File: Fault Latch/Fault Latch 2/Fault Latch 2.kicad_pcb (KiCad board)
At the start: 2 copper layers, 110 x 90 mm, 108 parts, among them K101 Fujitsu_FTR-LYAA005x, K102 Fujitsu_FTR-LYAA005x, K103 Fujitsu_FTR-LYAA005x, Q101 Q_NPN_BEC, Q102 Q_NPN_BEC, Q103 Q_NPN_BEC, Q104 Q_NPN_BEC, Q105 Q_NMOS_GSD, Q106 Q_NMOS_GSD, Q107 Q_PMOS_GSD, Q108 Q_PMOS_GSD, Q109 Q_NMOS_GDS, Q110 Q_NPN_BEC, Q111 Q_NPN_BEC, Q112 Q_NMOS_GSD, Q113 Q_PMOS_GSD, SW101 SW_Omron_B3FS, SW102 SW_Omron_B3FS, SW103 SW_Omron_B3FS, U101 SFH617A-1, U102 SFH617A-1, U103 SFH617A-1, U104 74AHC1G00, U105 74AHC1G00, U106 74AHC1G00, U107 74LS279, U108 641964-1, U109 SFH617A-1, U110 SFH617A-1, U111 641964-1, U112 641964-1, U113 641964-1, U114 641964-1, U115 641964-1, U116 641964-1, U117 74AHC1G00, U118 LM555xM, U119 74AHC1G00, U120 641964-1, U121 SFH617A-1, U122 641964-1

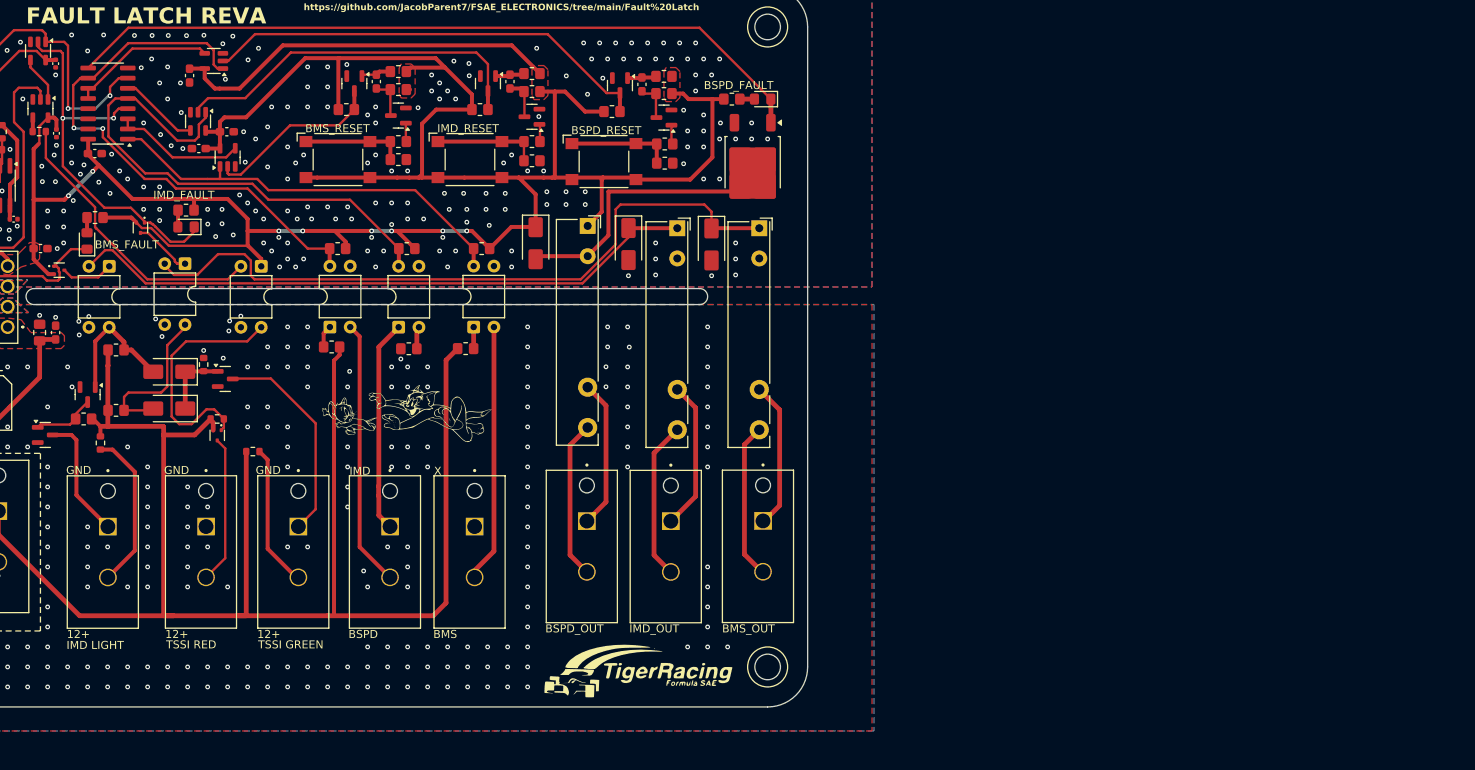
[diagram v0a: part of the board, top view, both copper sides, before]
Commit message: Fault Latch - THT
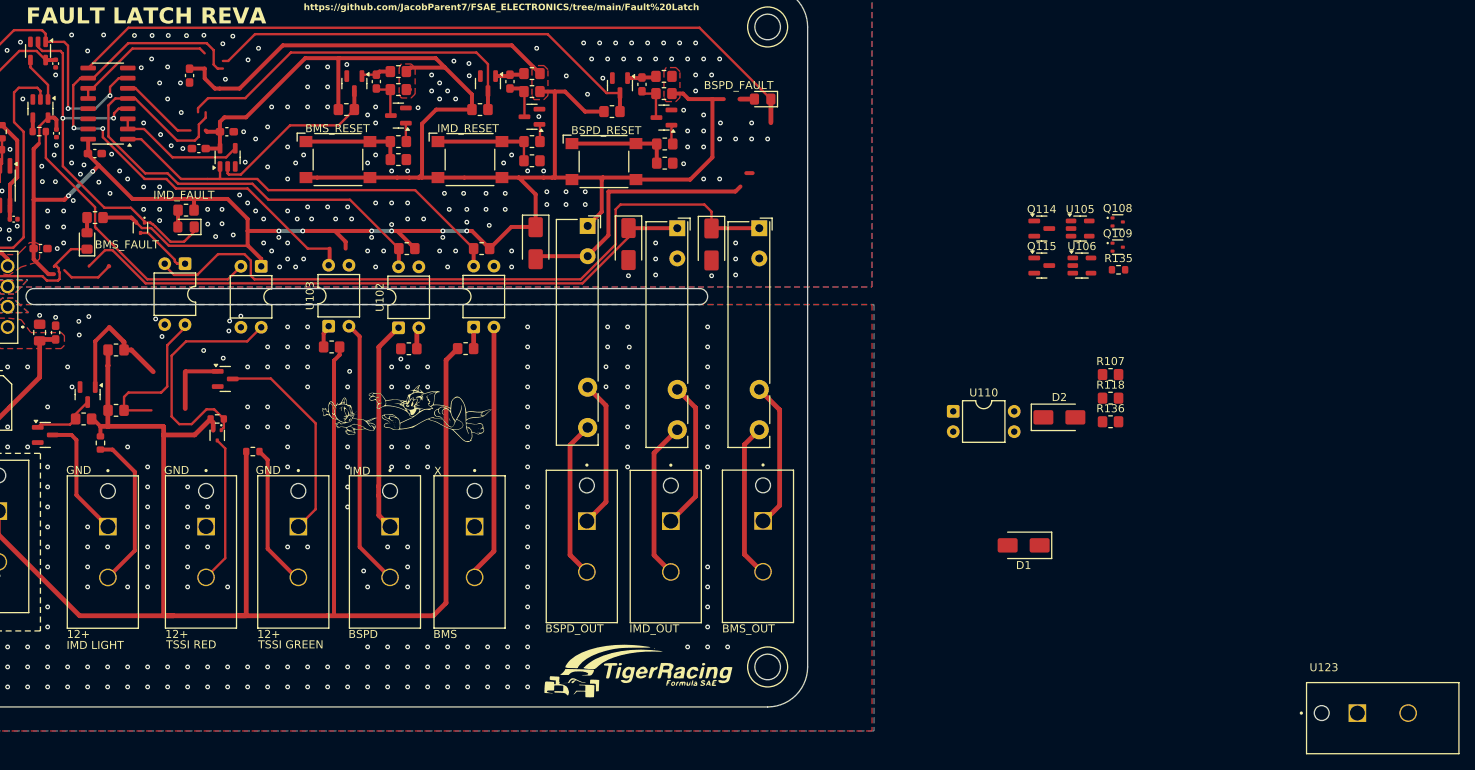
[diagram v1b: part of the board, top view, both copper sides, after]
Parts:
- removed D107, D108: D_Schottky, Diode_SMD:D_SMA
- removed R128: 10k, Resistor_SMD:R_0603_1608Metric
- added D1: SS12, Diode_SMD:D_SMA, F.Cu at (206.2, 113.9)
- added D2: SS12, Diode_SMD:D_SMA, F.Cu at (210.7, 97.9)
- added Q114: Q_NMOS_GSD, Package_TO_SOT_SMD:SOT-23, F.Cu at (208.5, 74.3)
- added Q115: Q_NMOS_GSD, Package_TO_SOT_SMD:SOT-23, F.Cu at (208.5, 78.9)
- added R135: 510R, Resistor_SMD:R_0603_1608Metric, F.Cu at (218.1, 79.4)
- added R136: 10k, Resistor_SMD:R_0805_2012Metric_Pad1.20x1.40mm_HandSolder, F.Cu at (217.1, 98.4)
- added U123: 641964-1, 641964-1:TE_641964-1, F.Cu at (247.9, 134.8)
- Q109: value Q_NMOS_GDS -> Q_PMOS_GSD; footprint Package_TO_SOT_SMD:TO-252-2 -> Package_TO_SOT_SMD:SOT-523
- R103: value 2.2k -> 10k
- R106, R107, R109: value 10k -> 1k
- R112: value 500R -> 510R
- R116, R117, R118: value 270R -> 2k
- moved Q108 132.4 mm to (218.0, 73.4)
- moved U106 111.5 mm to (213.5, 78.9), turned to 0 degrees
- moved U105 111.1 mm to (213.3, 74.3), turned to 0 degrees
- moved U110 107.0 mm to (197.4, 97.1), turned to 0 degrees
- moved R107 97.9 mm to (217.1, 92.5), turned to 0 degrees
- moved R118 60.3 mm to (217.1, 95.5), turned to 0 degrees
- moved Q109 46.8 mm to (218.0, 76.6), turned to 0 degrees
- moved U103 0.19 mm to (119.3, 86.5)
- moved U102 0.07 mm to (128.1, 86.7)
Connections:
- C113 pad 1: GNDPWR -> +12V
- C113 pad 2: +12V -> GNDPWR
- C114 pad 1: GNDPWR -> +12V
- C114 pad 2: +12V -> GNDPWR
- C115 pad 1: GNDPWR -> +12V
- C115 pad 2: +12V -> GNDPWR
- D105 pad 1: +5V -> Net-(D105-K)
- D105 pad 2: Net-(D105-A) -> GND
- K102 pad A1: +5V -> Net-(D105-K)
- K102 pad A2: Net-(D105-A) -> GND
- PS101 pad 1: +12V -> GNDPWR
- PS101 pad 2: GNDPWR -> +12V
- Q109 pad 2: Net-(D105-A) -> +5V
- Q109 pad 3: GND -> Net-(D105-K)
- R103 pad 1: Net-(R103-Pad1) -> +12V
- R103 pad 2: GNDPWR -> Net-(R103-Pad2)
- U102 pad 1: /IMD_HV -> Net-(R103-Pad2)
- U102 pad 2: Net-(R103-Pad1) -> /IMD_HV
- U120 pad 1: +12V -> GNDPWR
- U120 pad 2: GNDPWR -> +12V
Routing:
- net Net-(D105-A): track 33.4 -> 0.00 mm
- net GND: track 0.00 -> 32.6 mm
- net +12V: track 231.8 -> 234.6 mm
- net Net-(R103-Pad1): track 2.80 -> 0.00 mm
- net (no net): track 0.00 -> 0.80 mm

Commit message: Revised Fault Latch Layout
Fixed the schematic, did layout and wiring. Check for size and missed wires.
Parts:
- removed PS101: RI-1205S, DC-DC:RI0505S
- removed U108, U111, U112, U113, U114, U115, U116, U120, U123: 641964-1, 641964-1:TE_641964-1
- added J1: 1053141312, footprints:CONN_SD-105314-100_12_MOL, F.Cu at (-296.9, -371.2)
- added J2: 1053141106, molex.6-pin.footprint:CONN_SD-105314-100_06_MOL, F.Cu at (-301.6, -351.1)
- added J3: 1053131202, molex.2-pin.footprint:CONN_SD-105313-100_02_MOL, F.Cu at (-427.0, -311.3)
- added R137: 10k, Resistor_SMD:R_0805_2012Metric_Pad1.20x1.40mm_HandSolder, F.Cu at (-321.7, -358.5)
- added U1: LM1117DTX-5.0_NOPB, LM1117DTX-5.0_NOPB:TO228P970X238-3N, F.Cu at (-322.4, -324.9)
- R102, R103: value 10k -> 220; footprint Resistor_SMD:R_0805_2012Metric_Pad1.20x1.40mm_HandSolder -> Resistor_SMD:R_0201_0603Metric
- R104, R133: value 10k -> 220
- moved R107 739.7 mm to (-388.8, -331.7), turned to -90 degrees
- moved U105 731.8 mm to (-383.6, -349.2)
- moved R118 719.1 mm to (-361.6, -331.4), turned to 90 degrees
- moved U106 718.7 mm to (-382.8, -322.2)
- moved R136 712.7 mm to (-311.2, -380.0), turned to -90 degrees
- moved Q108 711.2 mm to (-353.1, -350.5)
- moved D1 711.2 mm to (-328.7, -354.8), turned to 0 degrees
- moved SW103 707.9 mm to (-433.8, -329.0), turned to 180 degrees
- moved R102 706.7 mm to (-398.1, -373.0), turned to 90 degrees
- moved R122 706.6 mm to (-429.3, -321.7), turned to -90 degrees
- moved U110 705.6 mm to (-348.0, -350.5)
- moved SW102 705.3 mm to (-433.0, -349.7), turned to 180 degrees
- moved SW101 705.3 mm to (-432.8, -371.7), turned to 180 degrees
- moved R123 704.6 mm to (-425.3, -326.5)
- moved R113 704.4 mm to (-429.0, -342.7), turned to -90 degrees
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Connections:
- C113 pad 2: GNDPWR -> GND
- C114 pad 2: GNDPWR -> GND
- C115 pad 2: GNDPWR -> GND
- K101 pad 13: Net-(K101-Pad13) -> /BMS Out
- K101 pad 14: Net-(K101-Pad14) -> /Shutdown Circuit In
- K102 pad 13: Net-(K102-Pad13) -> /Shutdown Circuit Out
- K102 pad 14: Net-(K102-Pad14) -> unconnected-(K102-Pad14)
- K103 pad 13: Net-(K103-Pad13) -> /IMD Out
- K103 pad 14: Net-(K103-Pad14) -> /IMD In
- Q105 pad 2: GNDPWR -> GND
- Q106 pad 2: GNDPWR -> GND
- Q106 pad 3: Net-(Q106-D) -> /IMD Light Out
- Q112 pad 2: GNDPWR -> GND
- Q112 pad 3: Net-(Q112-D) -> /TSSI Green Out
- Q114 pad 1: /BMS_GREEN -> /BMS_Green
- Q114 pad 2: GNDPWR -> GND
- Q115 pad 2: GNDPWR -> GND
- Q115 pad 3: Net-(Q115-D) -> /BMS Light Out
- R112 pad 2: Net-(R112-Pad2) -> /IMD Light In
- R130 pad 1: Net-(R130-Pad1) -> /TSSI Green In
- R135 pad 2: Net-(R135-Pad2) -> /BMS Light In
- U109 pad 3: GNDPWR -> GND
- U110 pad 3: GNDPWR -> GND
- U121 pad 3: GNDPWR -> GND
- U122 pad 1: GNDPWR -> GND
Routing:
- net +12V: track 234.6 -> 394.4 mm, vias 0 -> 31
- net /Shutdown Circuit Out: track 0.00 -> 85.8 mm
- net Net-(D104-K): track 87.5 -> 15.2 mm
- net Net-(D106-K): track 79.7 -> 16.9 mm
- net Net-(D103-K): track 94.1 -> 33.3 mm
- net +5V: track 406.5 -> 455.4 mm, vias 8 -> 28
- net /CLOCK: track 43.4 -> 88.8 mm
- net /TSSI Green Out: track 0.00 -> 43.4 mm, vias 0 -> 7
- net /BMS_SR: track 48.6 -> 90.8 mm, vias 2 -> 4
- net /NIMD_LV: track 65.6 -> 24.8 mm
- net /BMS Out: track 0.00 -> 37.3 mm, vias 0 -> 2
- net /IMD Out: track 0.00 -> 34.6 mm
- net /IMD Light Out: track 0.00 -> 34.2 mm, vias 0 -> 2
- net /BSPD_HV: track 33.4 -> 0.00 mm
- net GND: track 32.6 -> 0.00 mm, vias 218 -> 0
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- removed copper zone on B.Cu, net GNDPWR
- removed copper zone on F.Cu, net GNDPWR
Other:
- board size 110 x 90 mm -> 625.1 x 519.7 mm

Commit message: Fault Latch Layout revised
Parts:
- removed U1: LM1117DTX-5.0_NOPB, LM1117DTX-5.0_NOPB:TO228P970X238-3N
- removed U122: 641964-1, 641964-1:TE_641964-1
- added Q116: Q_NMOS_GSD, Package_TO_SOT_SMD:SOT-23, F.Cu at (230.8, 95.5)
- added R138: 10k, Resistor_SMD:R_0805_2012Metric_Pad1.20x1.40mm_HandSolder, F.Cu at (230.8, 100.2)
- added U2: LM1117DT-5.0, Package_TO_SOT_SMD:TO-252-3_TabPin2, F.Cu at (251.7, 118.0)
- R104: footprint Resistor_SMD:R_0805_2012Metric_Pad1.20x1.40mm_HandSolder -> Resistor_SMD:R_0201_0603Metric
- moved H101 873.7 mm to (270.4, 125.3)
- moved SW102 834.7 mm to (268.2, 103.1), turned to 90 degrees
- moved R114 828.8 mm to (265.7, 110.8), turned to 90 degrees
- moved SW101 823.3 mm to (268.1, 60.4), turned to 90 degrees
- moved R113 821.4 mm to (265.7, 95.5), turned to 90 degrees
- moved Q103 820.1 mm to (261.6, 110.7), turned to 180 degrees
- moved R115 819.4 mm to (261.6, 107.3), turned to 180 degrees
- moved R101 818.0 mm to (265.7, 67.7)
- moved C105 813.9 mm to (262.8, 103.6), turned to 90 degrees
- moved SW103 813.1 mm to (268.1, 81.5), turned to 90 degrees
- moved R119 811.0 mm to (261.6, 100.3), turned to 180 degrees
- moved R105 809.3 mm to (265.7, 53.0), turned to -90 degrees
- moved R123 806.3 mm to (265.7, 88.9), turned to 90 degrees
- moved R108 804.5 mm to (261.7, 55.9), turned to 180 degrees
- moved Q104 803.9 mm to (261.8, 96.9), turned to 90 degrees
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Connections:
- J1 pad 1: /NBMS HV -> GND
- J1 pad 10: /TSSI Red In -> /BPSD HV
- J1 pad 11: /TSSI Red Out -> /IMD HV
- J1 pad 12: unconnected-(J1-Pad12) -> /NBMS HV
- J1 pad 2: /IMD HV -> /BMS Light Out
- J1 pad 3: /BPSD HV -> /TSSI Green Out
- J1 pad 4: /BMS Light In -> /TSSI Green In
- J1 pad 5: /BMS Light Out -> /IMD Light Out
- J1 pad 7: /IMD Light Out -> unconnected-(J1-Pad7)
- J1 pad 8: /TSSI Green In -> /TSSI Red In
- J1 pad 9: /TSSI Green Out -> /BMS Light In
- J3 pad 1: +12V -> GND
- J3 pad 2: GND -> +12V
- K102 pad 14: unconnected-(K102-Pad14) -> /BPSD In
- Q112 pad 1: Net-(D1-A) -> Net-(Q112-G)
- Q113 pad 3: Net-(Q113-D) -> /TSSI Red In
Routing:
- net +12V: track 394.4 -> 202.0 mm, vias 31 -> 3
- net /CLOCK: track 88.8 -> 17.9 mm
- net /Shutdown Circuit Out: track 85.8 -> 36.4 mm
- net /BMS_Green: track 32.8 -> 79.2 mm
- net /TSSI Green Out: track 43.4 -> 4.45 mm, vias 7 -> 0
- net /Shutdown Circuit In: track 31.2 -> 65.2 mm, vias 2 -> 0
- net /BMS_SR: track 90.8 -> 59.4 mm, vias 4 -> 2
- net Net-(U106-Pad4): track 35.9 -> 4.56 mm, vias 2 -> 0
- net /IMD Light Out: track 34.2 -> 4.51 mm, vias 2 -> 0
- net /BPSD In: track 0.00 -> 28.1 mm
- net +5V: track 455.4 -> 430.5 mm, vias 28 -> 5
- net /IMD In: track 19.9 -> 41.0 mm
- net /BMS Out: track 37.3 -> 55.5 mm, vias 2 -> 0
- net Net-(U104-Pad4): track 22.1 -> 5.05 mm
- net /BMS Light Out: track 21.5 -> 5.02 mm, vias 2 -> 0
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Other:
- board size 625.1 x 519.7 mm -> 85 x 85 mm
- board text added: "FAULT LATCH"
- board text removed: "FAULT LATCH REVA"

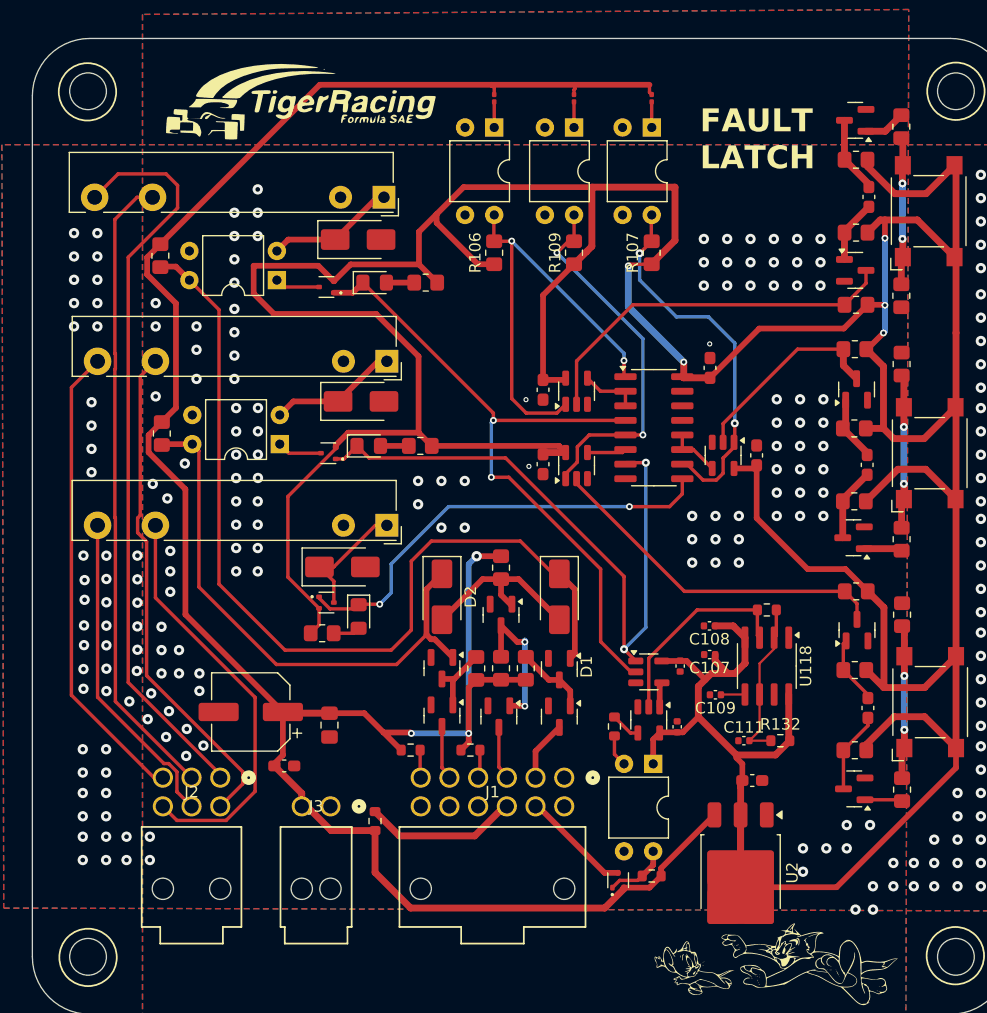
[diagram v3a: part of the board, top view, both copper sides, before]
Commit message: Fault Latch Updates
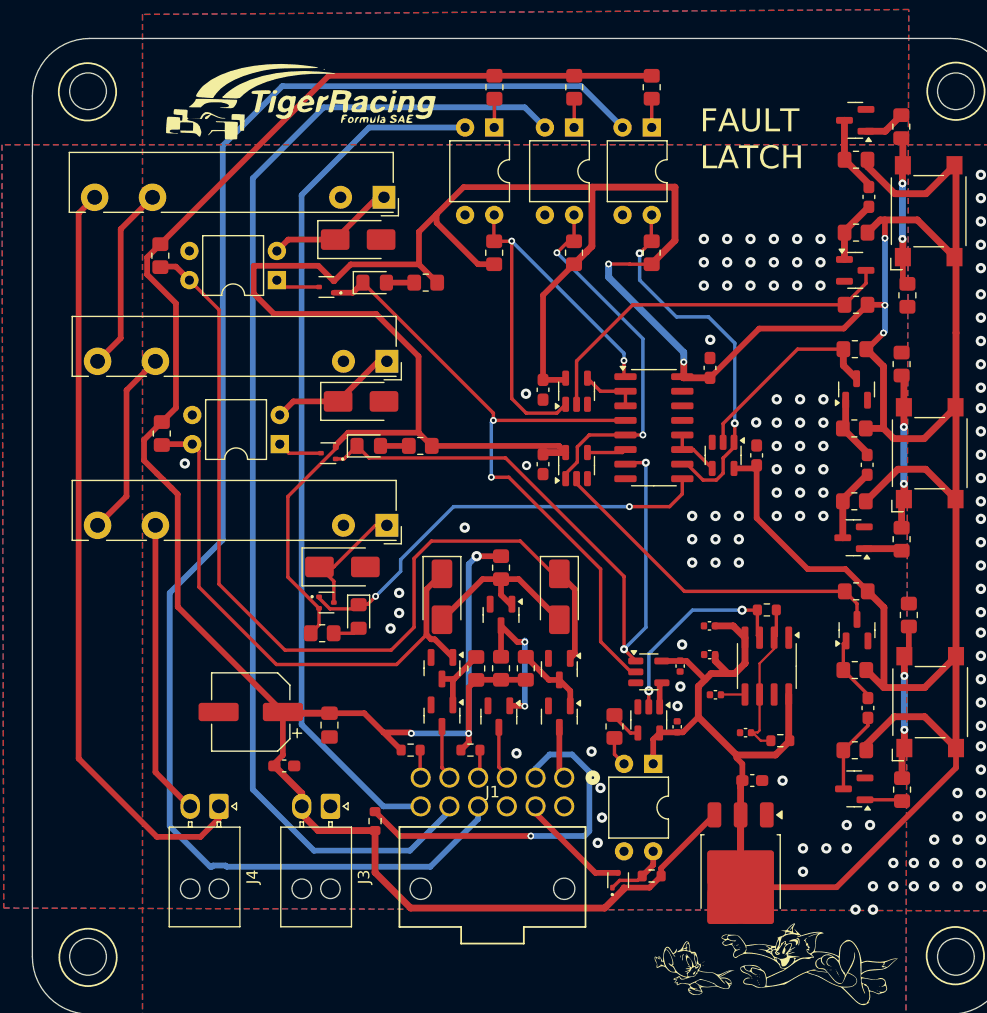
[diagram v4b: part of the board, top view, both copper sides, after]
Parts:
- removed J2: 1053141106, molex.6-pin.footprint:CONN_SD-105314-100_06_MOL
- added J4: 1053131202, Connector_Molex:Molex_Nano-Fit_105313-xx02_1x02_P2.50mm_Horizontal, F.Cu at (206.2, 112.2)
- J3: footprint molex.2-pin.footprint:CONN_SD-105313-100_02_MOL -> Connector_Molex:Molex_Nano-Fit_105313-xx02_1x02_P2.50mm_Horizontal
- R102, R103, R104: footprint Resistor_SMD:R_0201_0603Metric -> Resistor_SMD:R_0805_2012Metric_Pad1.20x1.40mm_HandSolder
- R133: footprint Resistor_SMD:R_0603_1608Metric -> Resistor_SMD:R_0805_2012Metric_Pad1.20x1.40mm_HandSolder
- moved R103 0.95 mm to (237.2, 49.6)
- moved R102 0.95 mm to (230.2, 49.6)
- moved R104 0.95 mm to (243.9, 49.6)
- moved C111 0.71 mm to (252.1, 105.8)
- moved R113 0.59 mm to (266.3, 95.5)
- moved R101 0.53 mm to (266.2, 67.7)
- turned J3 to -90 degrees
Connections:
- J1 pad 1: GND -> /BMS Light Out
- J1 pad 10: /BPSD HV -> /BSPD_HV
- J1 pad 11: /IMD HV -> /IMD_HV
- J1 pad 12: /NBMS HV -> /NBMS_HV
- J1 pad 2: /BMS Light Out -> /BMS Light In
- J1 pad 7: unconnected-(J1-Pad7) -> GND
- J1 pad 9: /BMS Light In -> unconnected-(J1-Pad9)
- K101 pad 13: /BMS Out -> Net-(K101-Pad13)
- K102 pad 14: /BPSD In -> Net-(K102-Pad14)
- K103 pad 13: /IMD Out -> Net-(K102-Pad14)
- K103 pad 14: /IMD In -> Net-(K101-Pad13)
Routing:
- net /BSPD_HV: track 0.00 -> 130.9 mm
- net /IMD_HV: track 0.00 -> 103.2 mm
- net /NBMS_HV: track 0.00 -> 76.1 mm
- net /BMS Out: track 55.5 -> 0.00 mm
- net /IMD Out: track 44.0 -> 0.00 mm
- net /IMD In: track 41.0 -> 0.00 mm
- net /BPSD In: track 28.1 -> 0.00 mm
- net /BMS Light In: track 13.5 -> 31.5 mm, vias 0 -> 1
- net Net-(K102-Pad14): track 0.00 -> 16.4 mm
- net Net-(K101-Pad13): track 0.00 -> 16.3 mm
- net /Shutdown Circuit Out: track 36.4 -> 25.8 mm
- net +5V: track 430.5 -> 433.1 mm
- net +12V: track 202.0 -> 200.8 mm
- net /Shutdown Circuit In: track 65.2 -> 66.2 mm
- net Net-(D103-K): track 39.1 -> 38.2 mm
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
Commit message: Fault Latch Layout Pre-Bom 2025 check
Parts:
- removed D1, D2: SS12, Diode_SMD:D_SMA
- added D107: D_Schottky, Diode_SMD:D_SMA, F.Cu at (225.6, 94.0)
- added D108: D_Schottky, Diode_SMD:D_SMA, F.Cu at (235.9, 93.9)
- R134: footprint Resistor_SMD:R_0603_1608Metric -> Resistor_SMD:R_0805_2012Metric_Pad1.20x1.40mm_HandSolder
- moved J4 2.64 mm to (205.9, 114.8), turned to 180 degrees
- moved R134 1.14 mm to (245.0, 118.5)
- moved H101 0.11 mm to (270.4, 125.2)
- moved H103 0.07 mm to (194.8, 50.0)
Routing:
- net /Shutdown Circuit Out: track 25.8 -> 29.5 mm
- net /Shutdown Circuit In: track 66.2 -> 69.8 mm
- net +12V: track 200.8 -> 203.0 mm
- net /IMD_HV: track 103.2 -> 105.0 mm
- net Net-(Q113-G): track 5.56 -> 6.25 mm
- net GND: vias 116 -> 367
- removed copper zone on F.Cu, net +12V
- removed copper zone on F.Cu, net +5V
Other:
- board text added: "https://github.com/LSUTigerRacing/Electronics"
- board text removed: "+12V"
- board text removed: "12+"
- board text removed: "BMS"
- board text removed: "BMS_OUT"
- board text removed: "BSPD"
- board text removed: "BSPD_OUT"
- board text removed: "GND"
- board text removed: "IMD"
- board text removed: "IMD LIGHT"
- board text removed: "IMD_OUT"
- board text removed: "TSSI GREEN"
- board text removed: "TSSI RED"
- board text removed: "X"
